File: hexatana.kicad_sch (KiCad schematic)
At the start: 66 parts, among them J1 USB_C_Receptacle_USB2.0, SW1 BOOT, SW1 SW_Push, SW10 SW_Push, SW11 SW_Push, SW12 SW_Push, SW13 SW_Push, SW14 SW_Push, SW15 SW_Push, SW16 SW_Push, SW17 SW_Push, SW18 SW_Push, SW19 SW_Push, SW2 RESET, SW2 SW_Push, SW20 SW_Push, SW21 SW_Push, SW22 SW_Push, SW23 SW_Push, SW24 SW_Push, SW25 SW_Push, SW26 SW_Push, SW27 SW_Push, SW28 SW_Push, SW29 SW_Push, SW3 SW_Push, SW30 SW_Push, SW31 SW_Push, SW32 SW_Push, SW33 SW_Push, SW34 SW_Push, SW37 SW_Push, SW38 SW_Push, SW4 SW_Push, SW5 SW_Push, SW6 SW_Push, SW7 SW_Push, SW8 SW_Push, SW9 SW_Push, U2 USBLC6-2SC6

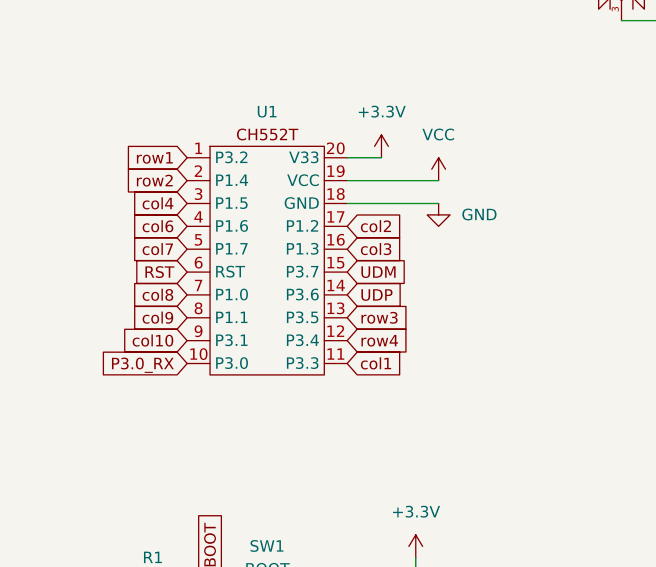
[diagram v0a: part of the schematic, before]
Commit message: fixed missing col5 on mcu
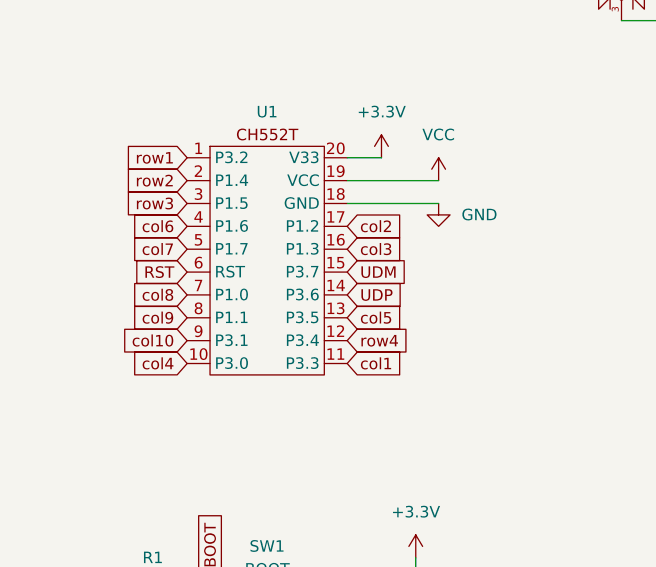
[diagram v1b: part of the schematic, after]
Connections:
- net P3.0_RX is gone; now on net col4: U1.10 (P3.0)
- net col4: no longer U1.3 (P1.5)
- net col5: now also U1.13 (P3.5)
- net row3: now also U1.3 (P1.5); no longer U1.13 (P3.5)
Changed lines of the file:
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@@
     )
   )
-  (global_label "P3.0_RX" (shape input) (at 52.07 142.24 180) (fields_autoplaced)
+  (global_label "col4" (shape input) (at 52.07 142.24 180) (fields_autoplaced)
     (effects (font (size 1.27 1.27)) (justify right))
-    (property "Intersheetrefs" "${INTERSHEET_REFS}" (at 41.3439 142.24 0)
+    (property "Intersheetrefs" "${INTERSHEET_REFS}" (at 44.9725 142.24 0)
       (effects (font (size 1.27 1.27)) (justify right) hide)
     )
@@
     )
   )
-  (global_label "col4" (shape input) (at 52.07 124.46 180) (fields_autoplaced)
+  (global_label "row3" (shape input) (at 52.07 124.46 180) (fields_autoplaced)
     (effects (font (size 1.27 1.27)) (justify right))
-    (property "Intersheetrefs" "${INTERSHEET_REFS}" (at 44.9725 124.46 0)
+    (property "Intersheetrefs" "${INTERSHEET_REFS}" (at 44.6096 124.46 0)
       (effects (font (size 1.27 1.27)) (justify right) hide)
     )
@@
     )
   )
-  (global_label "row3" (shape input) (at 69.85 137.16 0) (fields_autoplaced)
+  (global_label "col5" (shape input) (at 69.85 137.16 0) (fields_autoplaced)
     (effects (font (size 1.27 1.27)) (justify left))
-    (property "Intersheetrefs" "${INTERSHEET_REFS}" (at 77.3104 137.16 0)
+    (property "Intersheetrefs" "${INTERSHEET_REFS}" (at 76.9475 137.16 0)
       (effects (font (size 1.27 1.27)) (justify left) hide)
     )
